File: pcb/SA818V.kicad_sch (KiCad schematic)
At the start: 24 parts, among them J8 RF_SMA, Q12 BSS138, Q13 BSS138, U20 SA818S-V

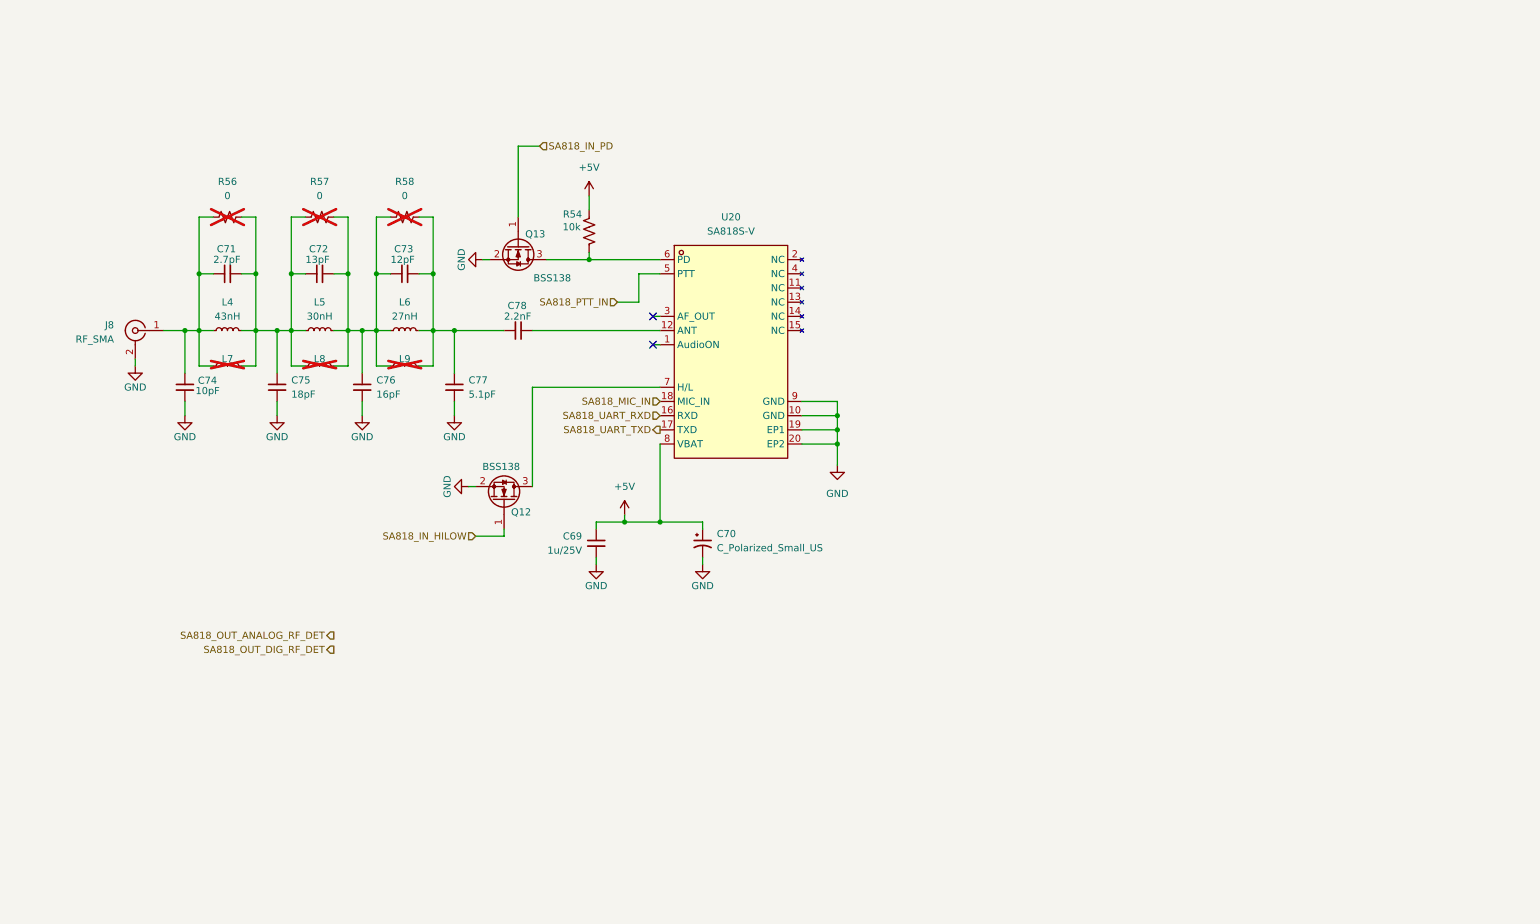
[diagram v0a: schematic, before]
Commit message: Move audio jack (J6) into SA818V sheet, rename nets/jumpers for clarity
Relocates the switched TRS jack from audio.kicad_sch into SA818V.kicad_sch
and updates the root sheet's pin interface to match (SA818_IN_MIC,
SA818_IN_PTT, new SA818_IN_PTT_HB), fixing an I2C_MIC_OUT/I2S_MIC_OUT
naming typo along the way. Ring/ring-switch/sleeve are wired; tip and
tip-switch (mic audio leg) are still open, per audio_ptt_path.md.

Also: renames GPS hierarchical labels and several power/regulation/
peripheral jumper values from generic (Jumper_2_Open, SolderJumper_2_Open)
to descriptive names, wires MCU_OUT_PTT_HB, and removes now-unused test
points/jumpers from the battery input sheets. Adds 74hc123_pinout.md
planning doc for the TX-safety timeout / force-off failsafe part.

Co-Authored-By: Claude Sonnet 5 <noreply@anthropic.com>
Claude-Session: https://claude.ai/code/session_01P3G1ionr2QCR8SZtKRreL3
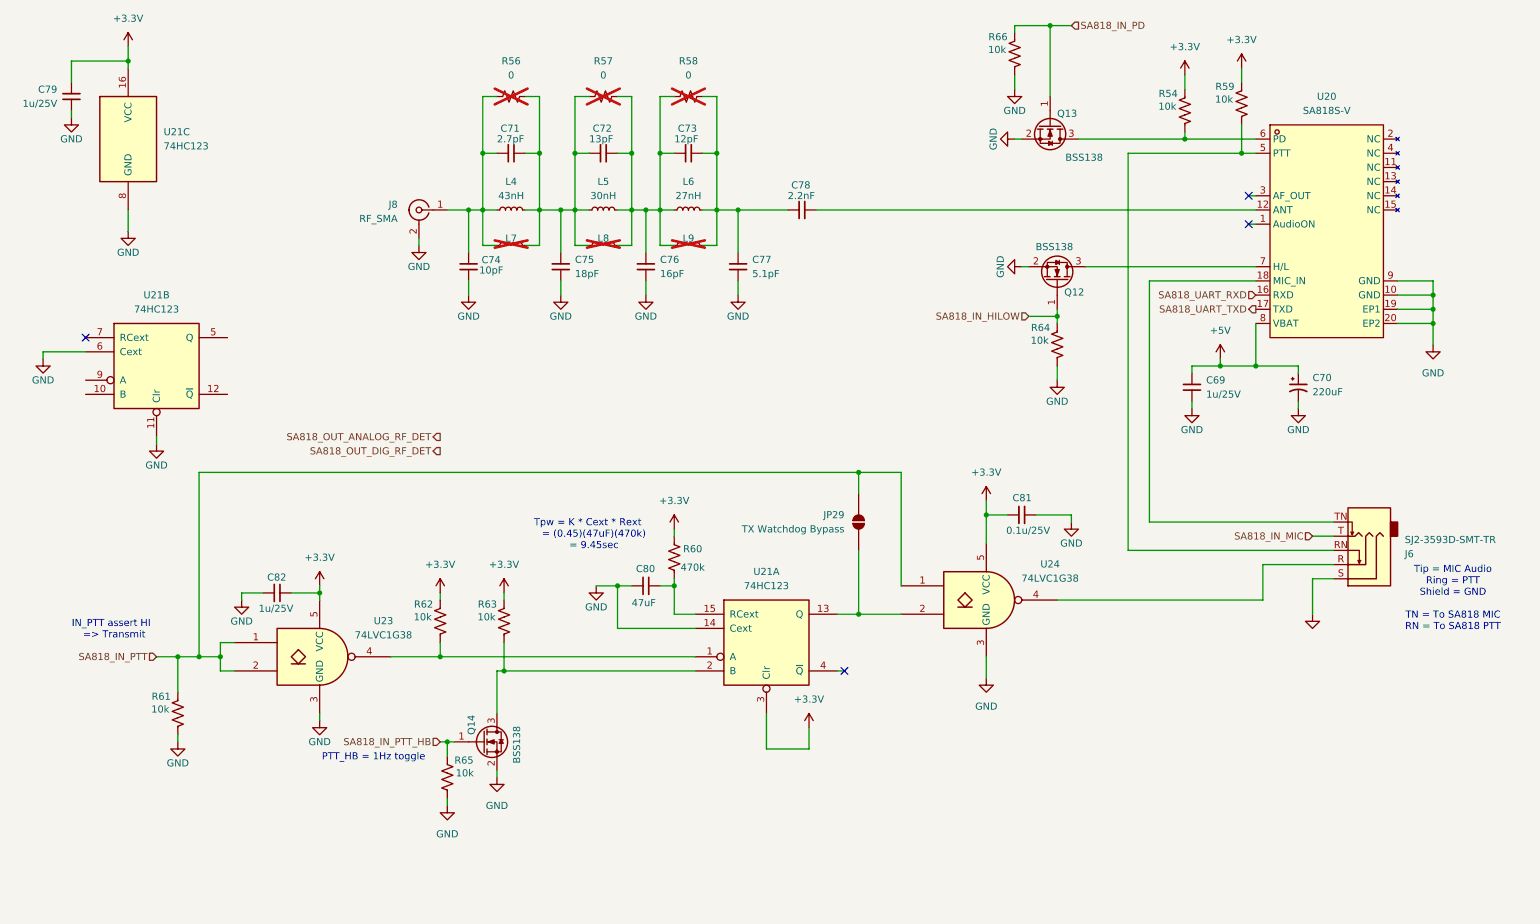
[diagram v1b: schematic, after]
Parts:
- added C79, C82: 1u/25V, Capacitor_SMD:C_0805_2012Metric, symbol Device:C_Small
- added C80: 47uF, Capacitor_SMD:C_1210_3225Metric, symbol Device:C_Small
- added C81: 0.1u/25V, Capacitor_SMD:C_0603_1608Metric, symbol Device:C_Small
- added J6: SJ2-3593D-SMT-TR, Connector_Audio:Jack_3.5mm_CUI_SJ2-3593D-SMT_Horizontal, symbol Connector_Audio:AudioJack3_SwitchTR
- added JP29: TX Watchdog Bypass, Jumper:SolderJumper-2_P1.3mm_Open_TrianglePad1.0x1.5mm, symbol Jumper:SolderJumper_2_Open
- added Q14: BSS138, Package_TO_SOT_SMD:SOT-23, symbol Transistor_FET:BSS138
- added R59, R61, R62, R63, R64, R65, R66: 10k, Resistor_SMD:R_0603_1608Metric, symbol Device:R_US
- added R60: 470k, Resistor_SMD:R_0603_1608Metric, symbol Device:R_US
- added U21: 74HC123, Package_SO:SOIC-16_3.9x9.9mm_P1.27mm, symbol 74xx:74HC123
- added U23, U24: 74LVC1G38, Package_TO_SOT_SMD:SOT-23-5, symbol 74xGxx:74LVC1G38
- C70: value C_Polarized_Small_US -> 220uF
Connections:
- net +5V: no longer R54.2
- net GND: now also C79.2, C80.1, C81.2, C82.2, J6.S, Q14.2 (S), R61.1, R64.1, R65.1, R66.1, U21.11 (Clr), U21.14 (Cext), U21.6 (Cext), U21.8 (GND), U23.3 (GND), U24.3 (GND)
- net SA818_IN_HILOW: now also R64.2
- net SA818_IN_PD: now also R66.2
- net SA818_MIC_IN: no longer names the net of U20.18 (MIC_IN)
- net SA818_MIC_IN: now also J6.TN
- net SA818_PTT_IN: no longer names the net of U20.5 (PTT)
- net SA818_PTT_IN: now also J6.RN, R59.1
- new net: JP29.1 (A), U21.13 (Q), U24.2
- new net: J6.R, U24.4
- new net: Q14.3 (D), R63.1, U21.2 (B)
- new net: C80.2, R60.2, U21.15 (RCext)
- new net: R62.1, U21.1 (A), U23.4
- new net +3.3V: C79.1, C81.1, C82.1, R54.2, R59.2, R60.1, R62.2, R63.2, U21.16 (VCC), U21.3 (Clr), U23.5 (VCC), U24.5 (VCC)
- new net SA818_IN_MIC: J6.T
- new net SA818_IN_PTT: JP29.2 (B), R61.2, U23.1, U23.2, U24.1
- new net SA818_IN_PTT_HB: Q14.1 (G), R65.2
- no-connect marks 2 -> 4
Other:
- note added: "IN_PTT assert HI => Transmit"
- note added: "PTT_HB = 1Hz toggle"
- note added: "Tip = MIC Audio Ring = PTT Shield = GND TN = To SA818 MIC RN = To SA818 PTT"
- note added: "Tpw = K * Cext * Rext = (0.45)(47uF)(470k) = 9.45sec"
- moved on the sheet: C69, C70, C71, C72, C73, C74, C75, C76, C77, C78, J8, L4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

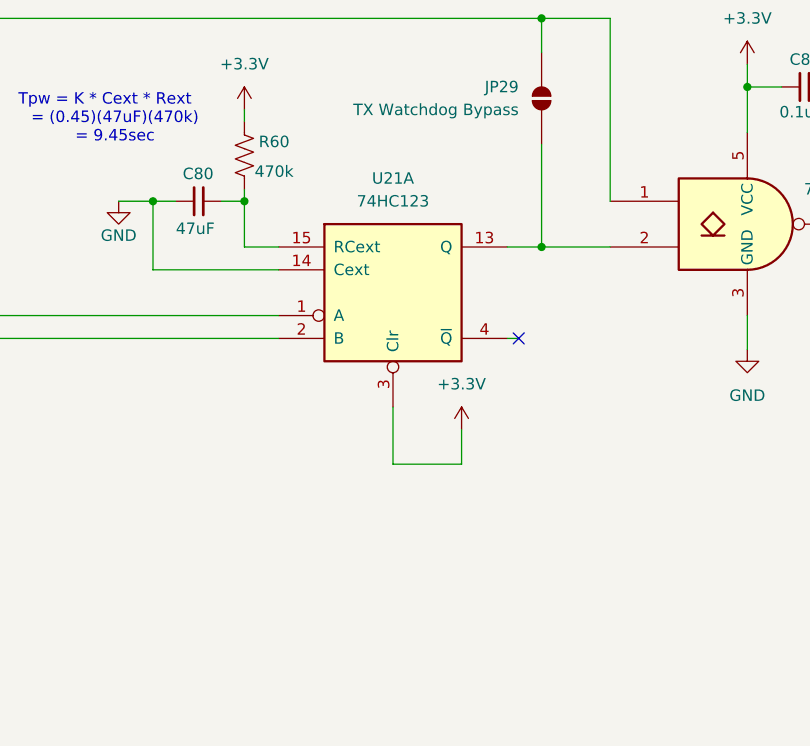
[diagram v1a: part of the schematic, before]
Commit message: Add power-up glitch guard (R67/C83/D13) on U21A's 1R̄D, doc + submodule bump
Implements Nexperia's Fig. 12 power-up circuit on U21 (74HC123) pin 3
(1R̄D), which was previously hard-tied to +3.3V: R67 (10k) charges C83
(0.1uF/25V) to hold reset briefly after power-up and block a spurious
TX-safety pulse from rail noise, and D13 (BAS116, reusing the same
part as D2/D3/D5) fast-discharges C83 on power-down so the guard is
reliable across quick power-cycles, not just cold boot.

Bumps the kicad_gx_library submodule pointer for the newly-imported
Vishay TMCMA1A476MTRF (47uF tantalum, C80's real sourced part) symbol/
footprint/3D model, committed and pushed there separately.

74hc123_pinout.md updated to record the built circuit (values, timing,
diode rationale) and correct a stale claim about pin 11's tie state.

Co-Authored-By: Claude Sonnet 5 <noreply@anthropic.com>
Claude-Session: https://claude.ai/code/session_01P3G1ionr2QCR8SZtKRreL3
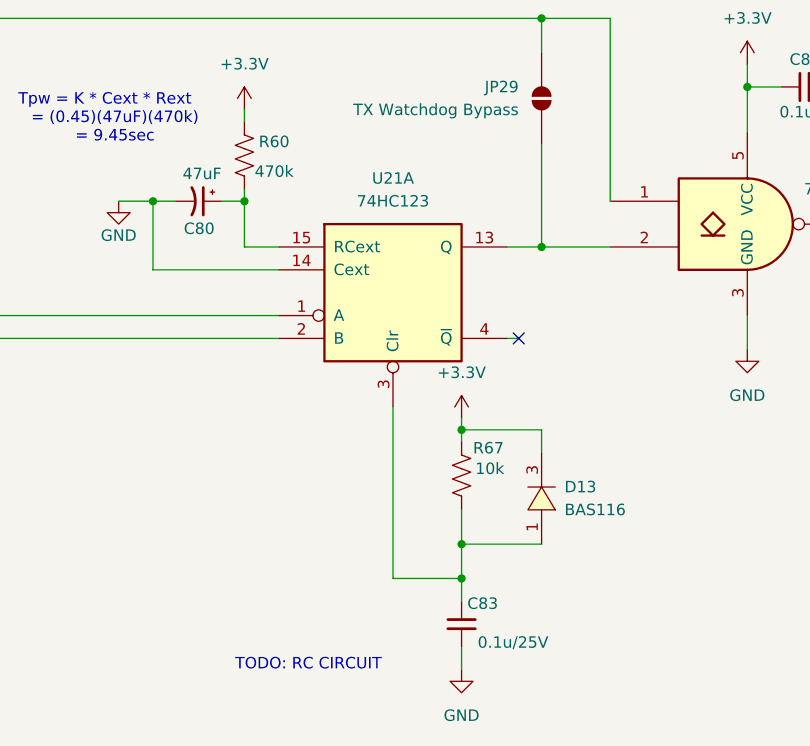
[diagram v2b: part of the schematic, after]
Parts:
- added C83: 0.1u/25V, Capacitor_SMD:C_0603_1608Metric, symbol Device:C_Small
- added D13: BAS116, kicad_gx_library:SOT-23_L2.9-W1.3-P1.90-LS2.4-BR, symbol kicad_gx_library:BAS116LT1G
- added R67: 10k, Resistor_SMD:R_0603_1608Metric, symbol Device:R_US
- C80: footprint Capacitor_SMD:C_1210_3225Metric -> kicad_gx_library:CP-SMD_1206_L3.2-W1.6-FD; symbol Device:C_Small -> Device:C_Polarized_Small_US; LCSC Part # C84494 -> C4984790; MPN GRM32ER71A476KE15L -> TMCMA1A476MTRF; Package 1210 -> 1206
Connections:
- net +3.3V: now also D13.3, R67.2; no longer U21.3 (Clr)
- net GND: now also C80.2, C83.1; no longer C80.1
- net at R60.2, U21.15 (RCext): now also C80.1; no longer C80.2
- new net: C83.2, D13.1, R67.1, U21.3 (Clr)
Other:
- note added: "TODO: RC CIRCUIT"
